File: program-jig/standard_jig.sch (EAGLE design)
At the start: 12 parts, among them J4 455-1750-1-ND, J5 6_PIN_SERIAL_CABLEPTH, U1 3.3V/150mA

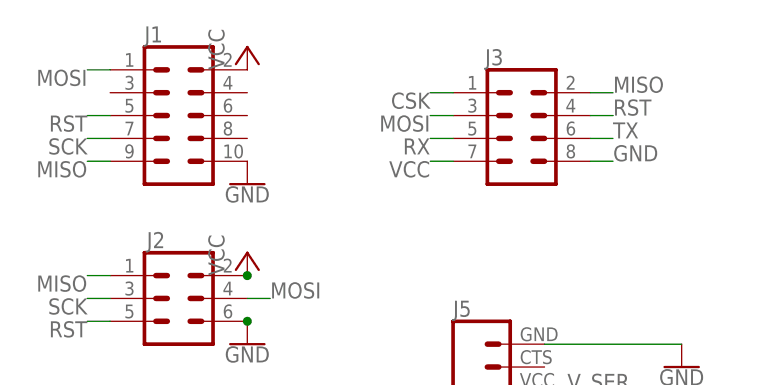
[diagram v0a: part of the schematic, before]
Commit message: Optional pullup on I2C + Default I2C0
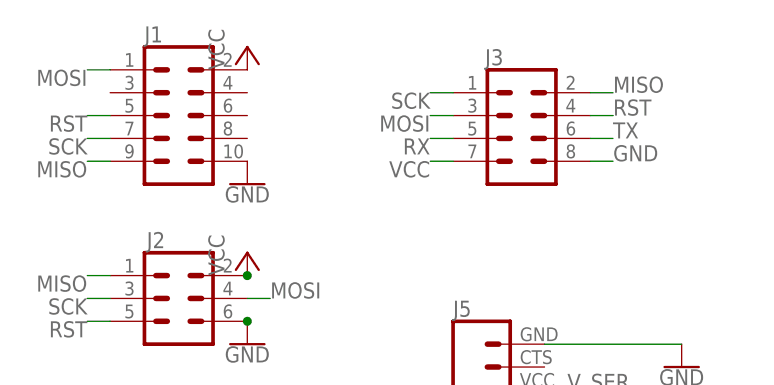
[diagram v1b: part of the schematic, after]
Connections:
- removed net CSK: J3.1
- net SCK: now also J3.1
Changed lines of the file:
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@@
 <?xml version="1.0" encoding="utf-8"?>
 <!DOCTYPE eagle SYSTEM "eagle.dtd">
-<eagle version="9.0.0">
+<eagle version="9.1.1">
 <drawing>
 <settings>
@@
 <label x="27.94" y="58.42" size="1.778" layer="95" rot="R180"/>
 </segment>
+<segment>
+<pinref part="J3" gate="G$1" pin="1"/>
+<wire x1="66.04" y1="63.5" x2="68.58" y2="63.5" width="0.1524" layer="91"/>
+<label x="66.04" y="63.5" size="1.778" layer="95" rot="R180"/>
+</segment>
 </net>
 <net name="RST" class="0">
@@
 </segment>
 </net>
-<net name="CSK" class="0">
-<segment>
-<pinref part="J3" gate="G$1" pin="1"/>
-<wire x1="66.04" y1="63.5" x2="68.58" y2="63.5" width="0.1524" layer="91"/>
-<label x="66.04" y="63.5" size="1.778" layer="95" rot="R180"/>
-</segment>
-</net>
